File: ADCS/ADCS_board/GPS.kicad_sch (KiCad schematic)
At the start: 5 parts, among them J7 Amphenol_901-144, J8 Amphenol_901-144, U12 Orion B16, U13 EP2W+

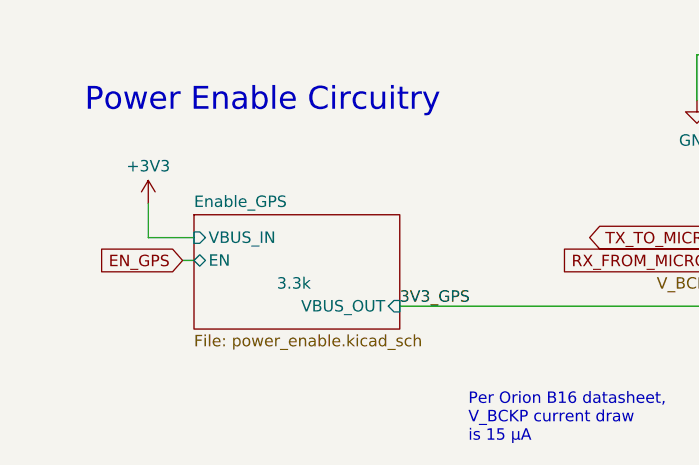
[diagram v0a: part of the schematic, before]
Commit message: main adcs board with initial traces coming out of MCU
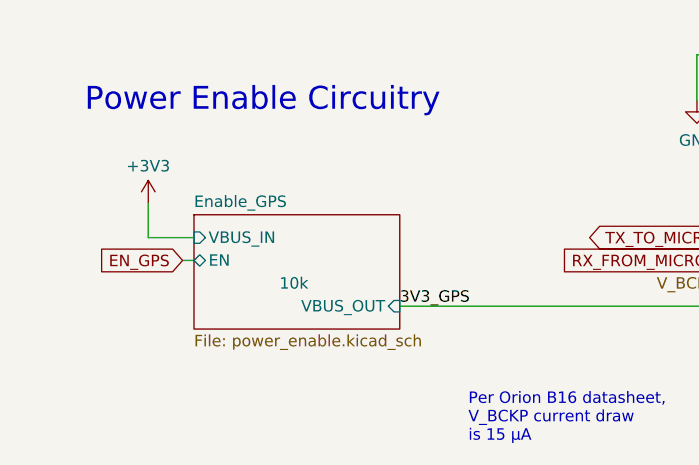
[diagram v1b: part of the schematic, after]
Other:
- title: (none) -> GPS
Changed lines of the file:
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@@
 	(paper "A4")
 	(title_block
+		(title "GPS")
+		(date "2025-02-05")
+		(rev "v1")
 		(company "Stanford Student Space Initiative")
+		(comment 1 "Sage Wu")
 	)
 	(junction
@@
 			)
 		)
-		(property "source_resistor" "3.3k"
+		(property "source_resistor" "10k"
 			(at 103.8098 118.11 0)
 			(show_name yes)
@@
 		)
 		(instances
-			(project "mainboard"
+			(project "ADCS_board"
 				(path "/db20b18b-d25a-428e-8229-70a189e1de75/0d8bb02c-6fa5-44fe-b4b4-1cd93a80e6f4"
 					(page "12")
